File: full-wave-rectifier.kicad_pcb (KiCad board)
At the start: 2 copper layers, 80.6 x 108 mm, 64 parts, among them J10 Control Right, J11 Main Right, J12 Power Connector, J2 Input Ch1, J3 Input Ch2, J4 Output Ch1, J5 Output Ch2, J6 Ochd input, J8 Control Left, J9 Main Left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

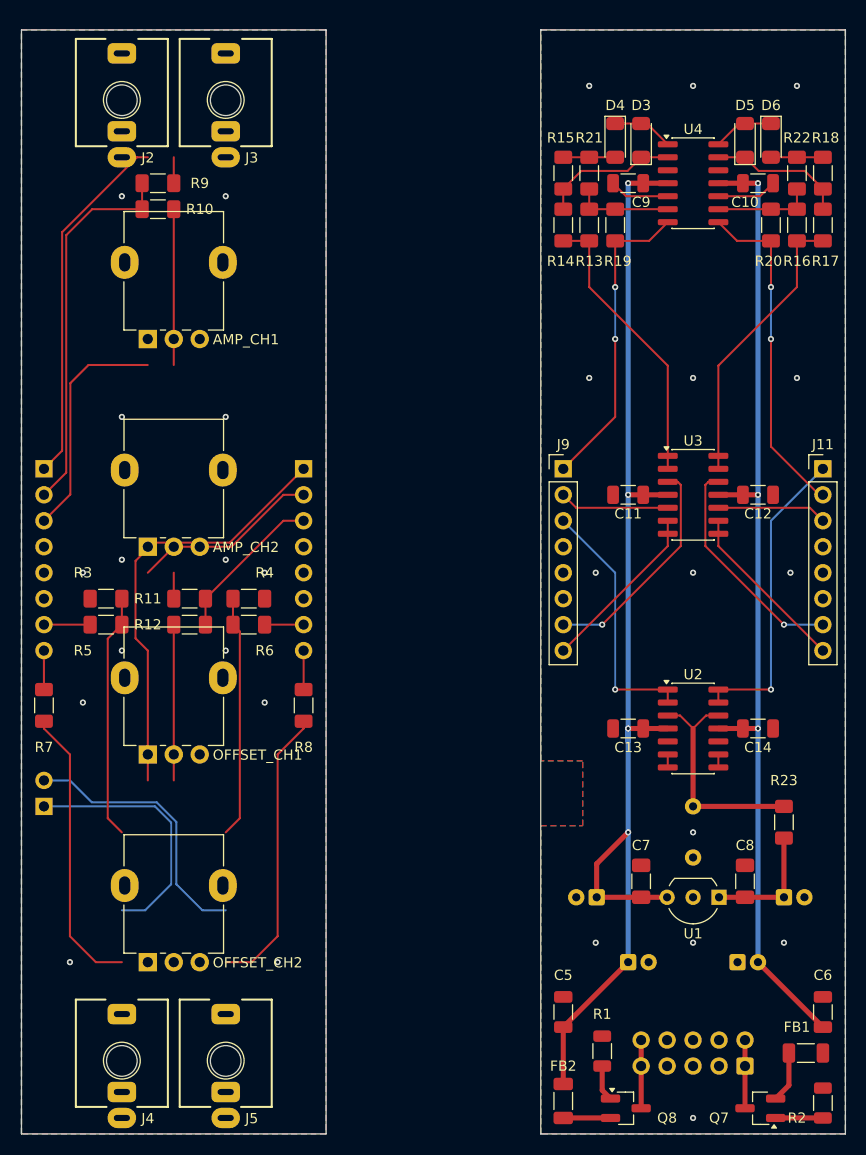
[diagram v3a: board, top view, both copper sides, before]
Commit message: Updated control panel
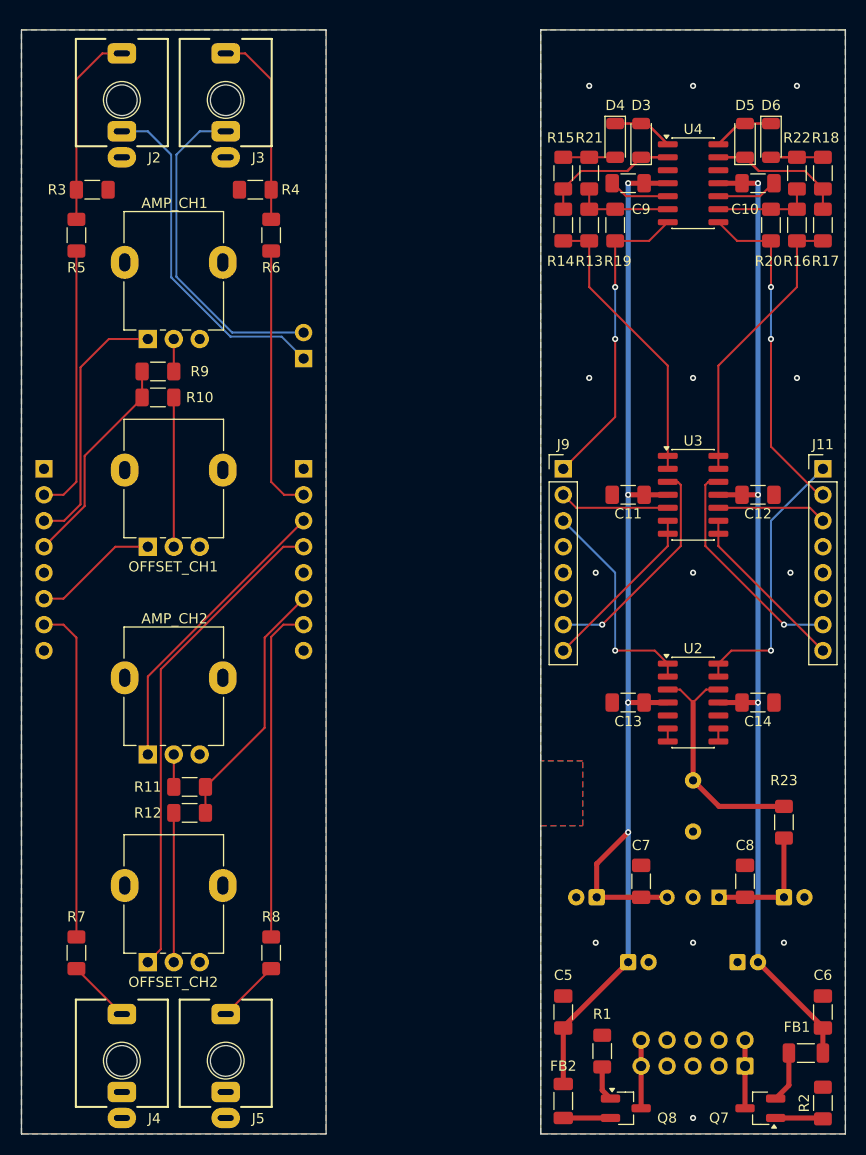
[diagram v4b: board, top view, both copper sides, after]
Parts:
- C10, C11, C12, C13, C14, C5, C6, C9: footprint Capacitor_SMD:C_1206_3216Metric -> Capacitor_SMD:C_1206_3216Metric_Pad1.33x1.80mm_HandSolder
- C15: value 1uF_Radial_TH -> 1uF
- R1, R2: footprint Resistor_SMD:R_1206_3216Metric -> Resistor_SMD:R_1206_3216Metric_Pad1.30x1.75mm_HandSolder
- R10, R11, R12, R13, R14, R15, R16, R17, R18, R19, R20, R3, R4, R9: value 100k_TH0.125 -> 100k
- R21, R22: value 51k_TH0.125 -> 51k
- R23: value 100Ω_TH0.125 -> 100
- R5, R6, R7, R8: value 1k_TH0.125 -> 1k
- U1: moved to B.Cu
- moved J6 50.6 mm to (139.7, 80.7)
- moved R3 40.0 mm to (119.0, 64.1), turned to 0 degrees
- moved R4 40.0 mm to (135.0, 64.1), turned to 180 degrees
- moved R5 38.2 mm to (117.5, 68.6), turned to -90 degrees
- moved R6 38.2 mm to (136.5, 68.6), turned to -90 degrees
- moved R7 24.4 mm to (117.5, 138.8)
- moved R8 24.4 mm to (136.5, 138.8)
- moved AMP_CH2 20.3 mm to (127.0, 119.4)
- moved OFFSET_CH1 20.3 mm to (127.0, 99.1)
- moved R11 18.4 mm to (128.6, 122.6)
- moved R9 18.4 mm to (125.5, 81.9)
- moved R10 18.4 mm to (125.5, 84.5)
- moved R12 18.4 mm to (128.6, 125.1)
- moved C13 2.54 mm to (171.4, 114.3)
- moved C14 2.54 mm to (184.2, 114.3)
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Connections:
- AMP_CH1 pad : (no net) -> GND
- AMP_CH1 pad 1: AMP_CH1 -> С_AMP_CH1
- AMP_CH2 pad : (no net) -> GND
- AMP_CH2 pad 1: AMP_CH2 -> С_AMP_CH2
- J10 pad 1: OFFSET_CH2 -> GND
- J10 pad 2: AMP_CH2 -> С_INPUT_CH2
- J10 pad 3: SUM_CH2 -> С_AMP_CH2
- J10 pad 4: GND -> С_OFFSET_CH2
- J10 pad 6: GND -> С_SUM_CH2
- J10 pad 7: INPUT_CH2 -> С_OUTPUT_CH2
- J10 pad 8: OUTPUT_CH2 -> GND
- J11 pad 1: OFFSET_CH2 -> GND
- J11 pad 2: AMP_CH2 -> M_INPUT_CH2
- J11 pad 3: SUM_CH2 -> M_AMP_CH2
- J11 pad 4: GND -> M_OFFSET_CH2
- J11 pad 6: GND -> M_SUM_CH2
- J11 pad 7: INPUT_CH2 -> M_OUTPUT_CH2
- J11 pad 8: OUTPUT_CH2 -> GND
- J8 pad 1: AMP_CH1 -> GND
- J8 pad 2: SUM_CH1 -> С_INPUT_CH1
- J8 pad 3: OFFSET_CH1 -> С_AMP_CH1
- J8 pad 4: GND -> С_SUM_CH1
- J8 pad 6: GND -> С_OFFSET_CH1
- J8 pad 7: INPUT_CH1 -> С_OUTPUT_CH1
- J8 pad 8: OUTPUT_CH1 -> GND
- J9 pad 1: AMP_CH1 -> GND
- J9 pad 2: SUM_CH1 -> M_INPUT_CH1
- J9 pad 3: OFFSET_CH1 -> M_AMP_CH1
- J9 pad 4: GND -> M_SUM_CH1
- J9 pad 6: GND -> M_OFFSET_CH1
- J9 pad 7: INPUT_CH1 -> M_OUTPUT_CH1
- J9 pad 8: OUTPUT_CH1 -> GND
- OFFSET_CH1 pad : (no net) -> GND
- OFFSET_CH1 pad 1: OFFSET_CH1 -> С_OFFSET_CH1
- OFFSET_CH2 pad : (no net) -> GND
- OFFSET_CH2 pad 1: OFFSET_CH2 -> С_OFFSET_CH2
- R10 pad 1: SUM_CH1 -> С_SUM_CH1
- R11 pad 2: SUM_CH2 -> С_SUM_CH2
- R12 pad 1: SUM_CH2 -> С_SUM_CH2
- R19 pad 2: AMP_CH1 -> M_AMP_CH1
- R20 pad 2: AMP_CH2 -> M_AMP_CH2
- R5 pad 2: INPUT_CH1 -> С_INPUT_CH1
- R6 pad 2: INPUT_CH2 -> С_INPUT_CH2
- R7 pad 1: OUTPUT_CH1 -> С_OUTPUT_CH1
- R8 pad 1: OUTPUT_CH2 -> С_OUTPUT_CH2
- R9 pad 2: SUM_CH1 -> С_SUM_CH1
- U2 pad 1: OFFSET_CH1 -> M_OFFSET_CH1
- U2 pad 13: OFFSET_CH2 -> M_OFFSET_CH2
- U2 pad 14: OFFSET_CH2 -> M_OFFSET_CH2
- U2 pad 2: OFFSET_CH1 -> M_OFFSET_CH1
- U3 pad 10: SUM_CH2 -> M_SUM_CH2
- U3 pad 12: INPUT_CH2 -> M_INPUT_CH2
- U3 pad 3: INPUT_CH1 -> M_INPUT_CH1
- U3 pad 5: SUM_CH1 -> M_SUM_CH1
- U3 pad 6: OUTPUT_CH1 -> M_OUTPUT_CH1
- U3 pad 7: OUTPUT_CH1 -> M_OUTPUT_CH1
- U3 pad 8: OUTPUT_CH2 -> M_OUTPUT_CH2
- U3 pad 9: OUTPUT_CH2 -> M_OUTPUT_CH2
- U4 pad 7: AMP_CH1 -> M_AMP_CH1
- U4 pad 8: AMP_CH2 -> M_AMP_CH2
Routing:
- net OFFSET_CH2: track 72.3 -> 0.00 mm, vias 1 -> 0
- net AMP_CH1: track 65.6 -> 0.00 mm, vias 2 -> 0
- net (no net): track 0.00 -> 54.6 mm, vias 0 -> 2
- net AMP_CH2: track 51.4 -> 0.00 mm, vias 2 -> 0
- net С_OFFSET_CH2: track 0.00 -> 48.1 mm
- net SUM_CH1: track 48.1 -> 0.00 mm
- net OFFSET_CH1: track 47.9 -> 0.00 mm, vias 1 -> 0
- net GND: track 11.8 -> 59.0 mm, vias 29 -> 15
- net M_AMP_CH2: track 0.00 -> 33.1 mm, vias 0 -> 2
- net С_OUTPUT_CH2: track 0.00 -> 33.0 mm
- net С_OUTPUT_CH1: track 0.00 -> 33.0 mm
- net С_AMP_CH2: track 0.00 -> 29.2 mm
- net M_OFFSET_CH2: track 0.00 -> 26.8 mm, vias 0 -> 1
- net INPUT_CH1: track 26.6 -> 0.00 mm, vias 1 -> 0
- net С_INPUT_CH1: track 0.00 -> 26.3 mm
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
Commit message: Updated layout
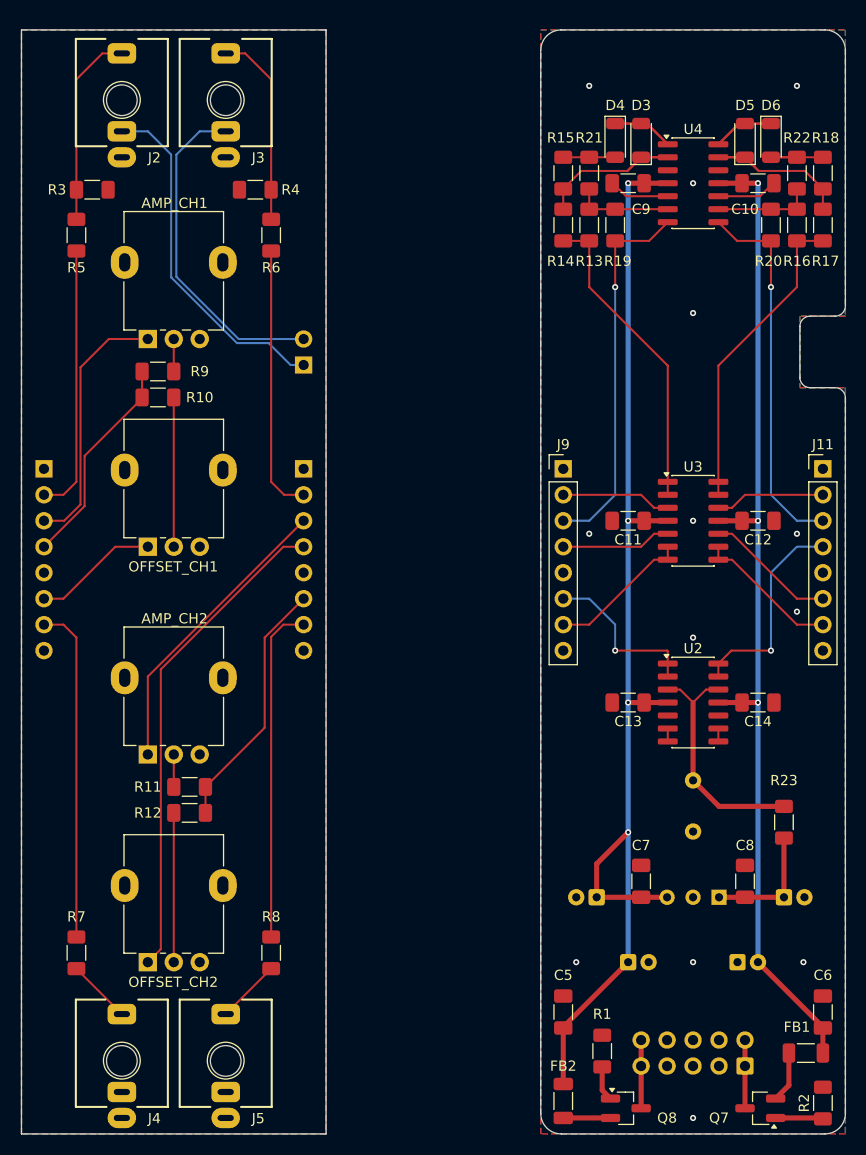
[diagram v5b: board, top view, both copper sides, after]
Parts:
- moved C11 2.54 mm to (171.4, 96.5)
- moved C12 2.54 mm to (184.2, 96.5)
- moved U3 2.54 mm to (177.8, 96.5)
- moved J6 0.63 mm to (139.7, 81.3)
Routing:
- net (no net): track 54.6 -> 0.00 mm, vias 2 -> 0
- net GND: track 59.0 -> 11.8 mm, vias 15 -> 13
- net M_AMP_CH1: track 0.00 -> 36.9 mm, vias 0 -> 1
- net M_OFFSET_CH1: track 0.00 -> 16.3 mm, vias 0 -> 1
- net M_OUTPUT_CH1: track 0.00 -> 14.1 mm
- net M_INPUT_CH2: track 22.1 -> 10.8 mm, vias 1 -> 0
- net M_SUM_CH1: track 0.00 -> 10.8 mm
- net M_INPUT_CH1: track 0.00 -> 10.8 mm
- net M_OFFSET_CH2: track 26.8 -> 20.7 mm
- net M_AMP_CH2: track 33.1 -> 36.9 mm, vias 2 -> 1
- net M_OUTPUT_CH2: track 16.9 -> 14.1 mm
- net Net-(U3D--): track 28.0 -> 30.6 mm
- net Net-(U3A--): track 28.0 -> 30.6 mm
- net M_SUM_CH2: track 10.8 -> 12.9 mm
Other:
- outline, holes or cut-outs redrawn

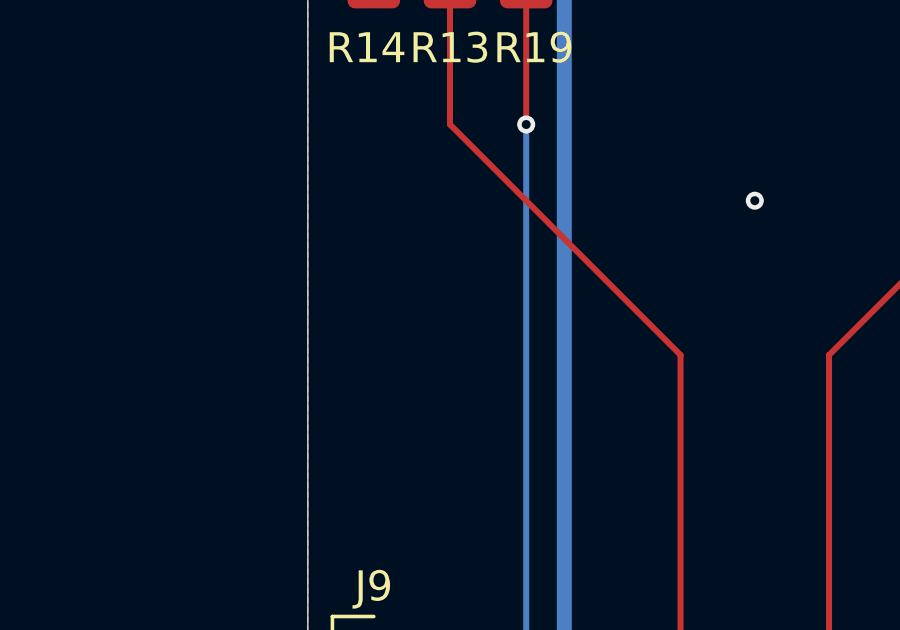
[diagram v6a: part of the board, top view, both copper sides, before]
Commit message: Added test point
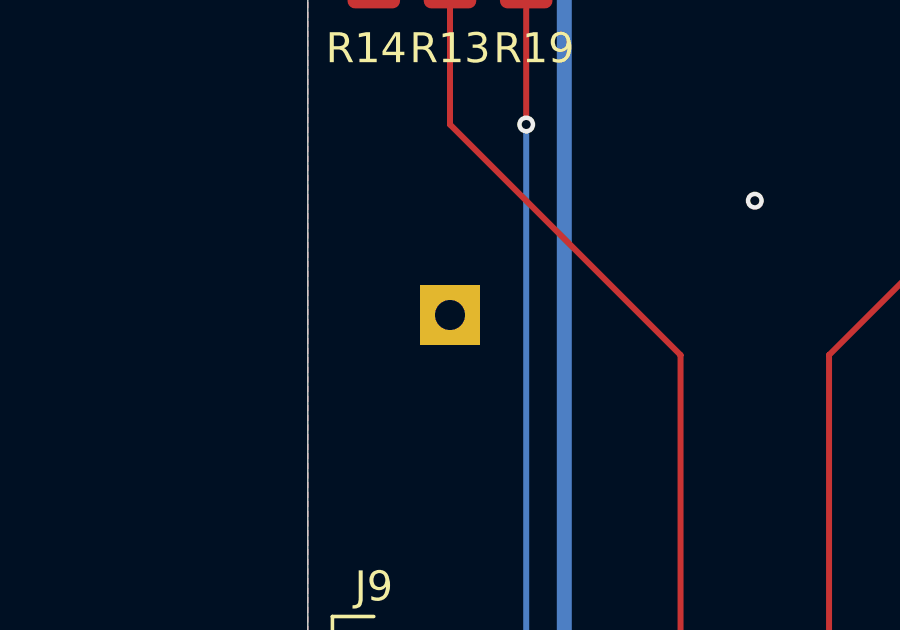
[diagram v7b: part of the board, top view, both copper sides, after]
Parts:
- added TP1: TestPoint, TestPoint:TestPoint_THTPad_2.0x2.0mm_Drill1.0mm, B.Cu at (167.6, 80.0)
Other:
- board text added: "GND"
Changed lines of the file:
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@@
 		)
+	)
+	(footprint "TestPoint:TestPoint_THTPad_2.0x2.0mm_Drill1.0mm"
+		(layer "B.Cu")
+		(at 167.64 80.01 180)
+		(descr "THT rectangular pad as test Point, square 2.0mm_Drill1.0mm  side length, hole diameter 1.0mm")
+		(tags "test point THT pad rectangle square")
+		(property "Reference" "TP1"
+			(at 0 1.998 0)
+			(layer "B.SilkS")
+			(hide yes)
+			(effects
+				(font
+					(size 1 1)
+					(thickness 0.15)
+				)
+				(justify mirror)
+			)
+		)
+		(property "Value" "TestPoint"
+			(at 0 -2.05 0)
+			(layer "B.Fab")
+			(effects
+				(font
+					(size 1 1)
+					(thickness 0.15)
+				)
+				(justify mirror)
+			)
+		)
+		(property "Datasheet" "~"
+			(at 0 0 0)
+			(unlocked yes)
+			(layer "B.Fab")
+			(hide yes)
+			(effects
+				(font
+					(size 1.27 1.27)
+					(thickness 0.15)
+				)
+				(justify mirror)
+			)
+		)
+		(property "Description" "test point"
+			(at 0 0 0)
+			(unlocked yes)
+			(layer "B.Fab")
+			(hide yes)
+			(effects
+				(font
+					(size 1.27 1.27)
+					(thickness 0.15)
+				)
+				(justify mirror)
+			)
+		)
+		(property ki_fp_filters "Pin* Test*")
+		(sheetname "/Power/")
+		(sheetfile "power.kicad_sch")
+		(attr exclude_from_pos_files)
+		(fp_line
+			(start 1.2 1.2)
+			(end 1.2 -1.2)
+			(stroke
+				(width 0.12)
+				(type solid)
+			)
+			(layer "B.SilkS")
+		)
+		(fp_line
+			(start 1.2 -1.2)
+			(end -1.2 -1.2)
+			(stroke
+				(width 0.12)
+				(type solid)
+			)
+			(layer "B.SilkS")
+		)
+		(fp_line
+			(start -1.2 1.2)
+			(end 1.2 1.2)
+			(stroke
+				(width 0.12)
+				(type solid)
+			)
+			(layer "B.SilkS")
+		)
+		(fp_line
+			(start -1.2 -1.2)
+			(end -1.2 1.2)
+			(stroke
+				(width 0.12)
+				(type solid)
+			)
+			(layer "B.SilkS")
+		)
+		(fp_line
+			(start 1.5 -1.5)
+			(end 1.5 1.5)
+			(stroke
+				(width 0.05)
+				(type solid)
+			)
+			(layer "B.CrtYd")
+		)
+		(fp_line
+			(start 1.5 -1.5)
+			(end -1.5 -1.5)
+			(stroke
+				(width 0.05)
+				(type solid)
+			)
+			(layer "B.CrtYd")
+		)
+		(fp_line
+			(start -1.5 1.5)
+			(end 1.5 1.5)
+			(stroke
+				(width 0.05)
+				(type solid)
+			)
+			(layer "B.CrtYd")
+		)
+		(fp_line
+			(start -1.5 1.5)
+			(end -1.5 -1.5)
+			(stroke
+				(width 0.05)
+				(type solid)
+			)
+			(layer "B.CrtYd")
+		)
+		(fp_text user "${REFERENCE}"
+			(at 0 2 0)
+			(layer "B.Fab")
+			(effects
+				(font
+					(size 1 1)
+					(thickness 0.15)
+				)
+				(justify mirror)
+			)
+		)
+		(pad "1" thru_hole rect
+			(at 0 0 180)
+			(size 2 2)
+			(drill 1)
+			(layers "*.Cu" "*.Mask")
+			(remove_unused_layers no)
+			(net 1 "GND")
+			(pinfunction "1")
+			(pintype "passive")
+		)
+		(embedded_fonts no)
 	)
 	(footprint "Connector_PinSocket_2.54mm:PinSocket_1x08_P2.54mm_Vertical"
@@
 		(layer "User.1")
 	)
+	(gr_text "GND"
+		(at 167.64 83.185 0)
+		(layer "B.SilkS")
+		(effects
+			(font
+				(size 1 1)
+				(thickness 0.15)
+			)
+			(justify bottom mirror)
+		)
+	)
 	(segment

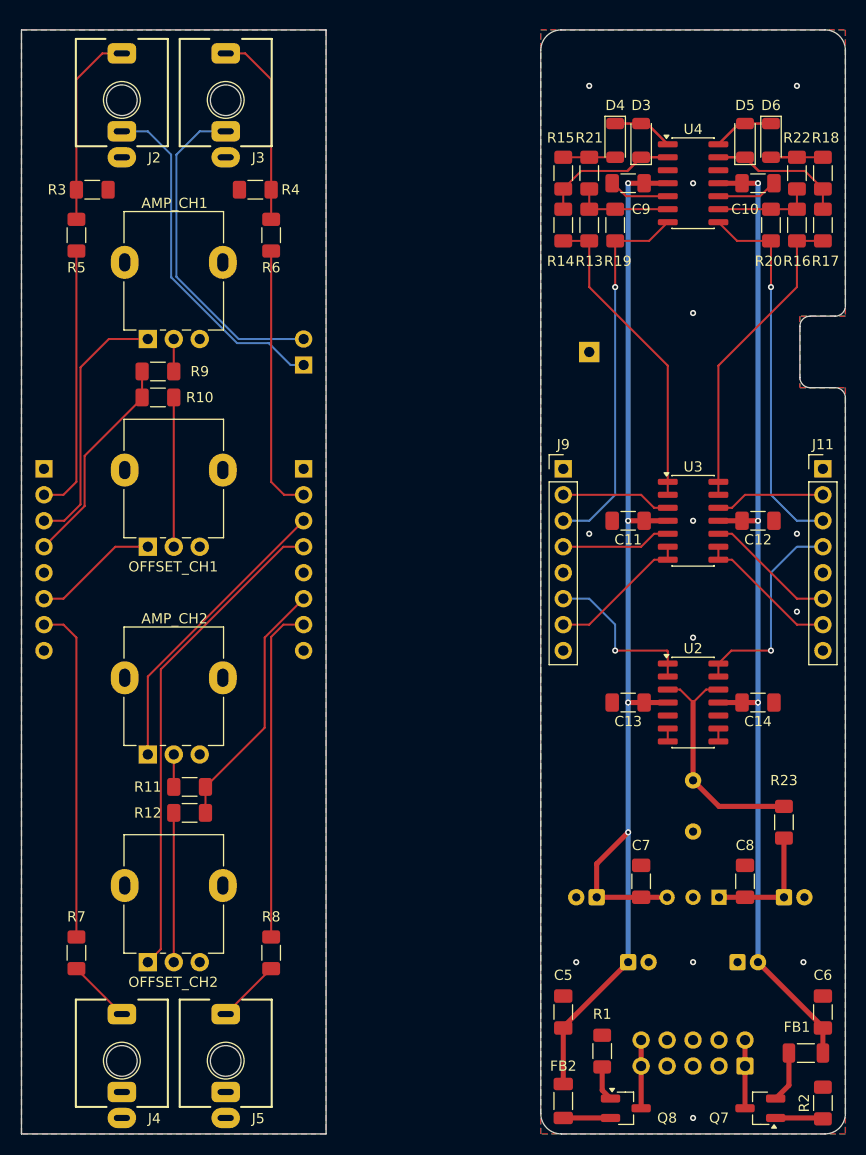
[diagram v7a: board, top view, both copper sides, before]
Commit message: fixed traces width
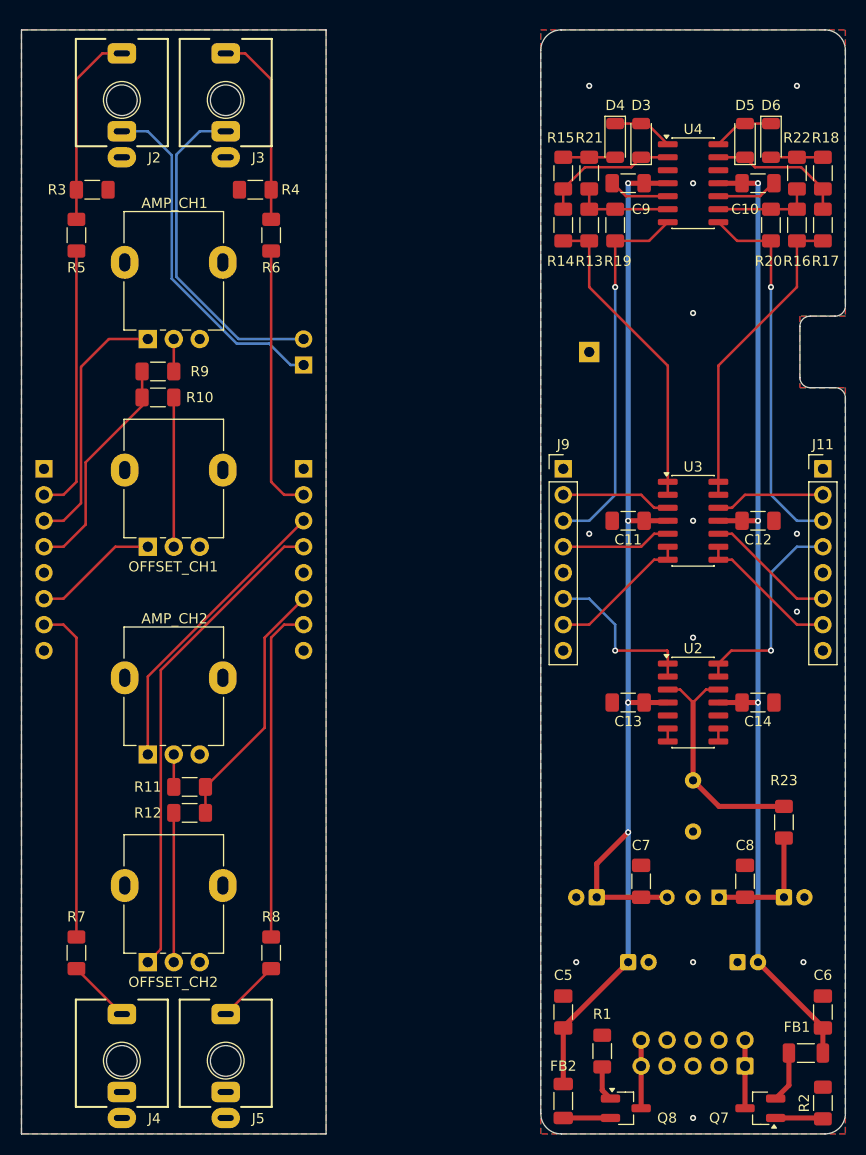
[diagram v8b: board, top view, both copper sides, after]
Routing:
- net С_SUM_CH1: track 21.1 -> 22.2 mm
